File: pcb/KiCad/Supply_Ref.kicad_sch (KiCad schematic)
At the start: 39 parts, among them J9 RF_Shield_One_Piece, U1 LT3045EMSE, U2 LT3094EMSE, U3 LT1236-10, U6 LT8610

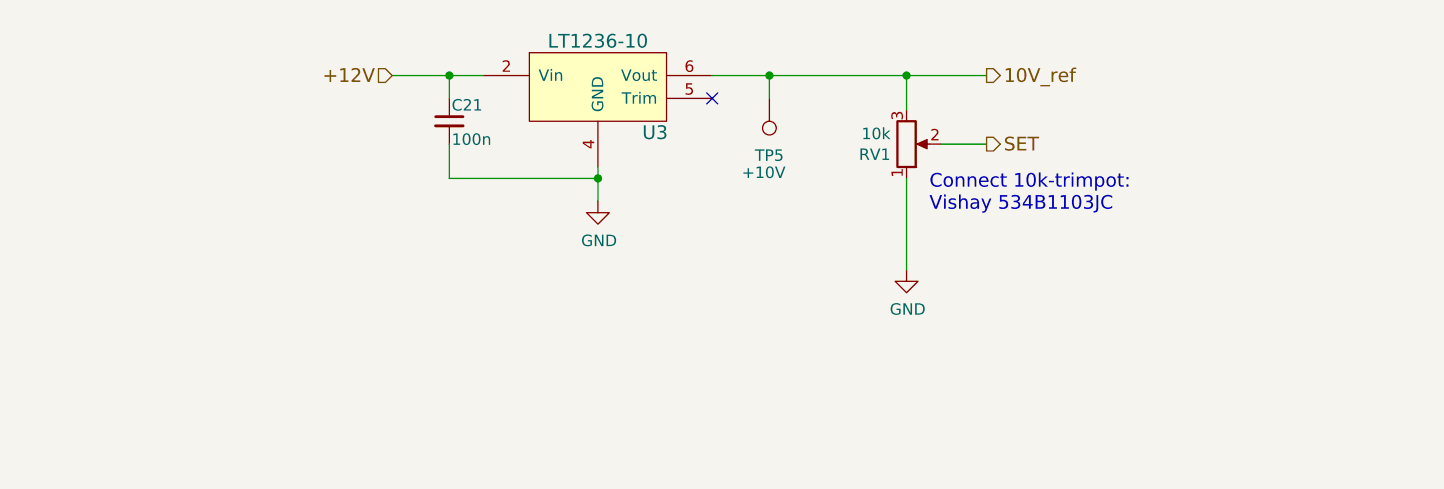
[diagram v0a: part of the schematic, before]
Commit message: Updated to KiCad 8
Added assembly instructions for the potentiometer
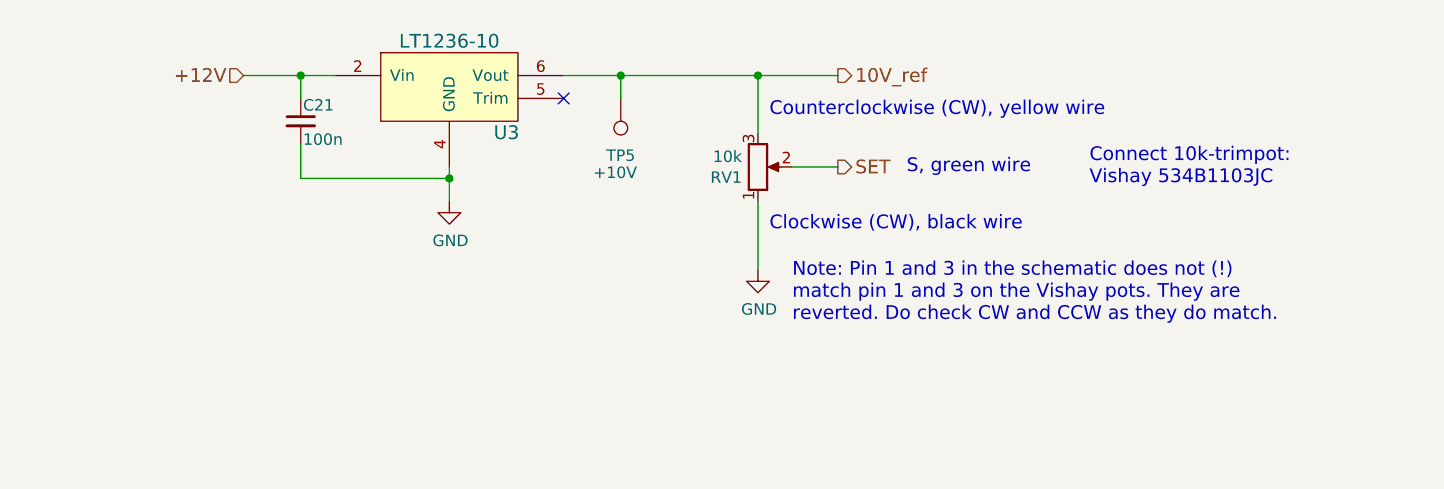
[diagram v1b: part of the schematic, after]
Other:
- note added: "Clockwise (CW), black wire"
- note added: "Counterclockwise (CW), yellow wire"
- note added: "Note: Pin 1 and 3 in the schematic does not (!) match pin 1 and 3 on the Vishay pots. They are reverted. Do check CW and CCW as they do match."
- note added: "S, green wire"
- moved on the sheet: C21, RV1, TP5, U3
